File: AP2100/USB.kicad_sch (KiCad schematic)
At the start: 40 parts, among them IC9 MAX1564ETE+, J7 SS-52000-001, U10 LS1043ASE7KQB-Layerscape, U22 74LVC2G04

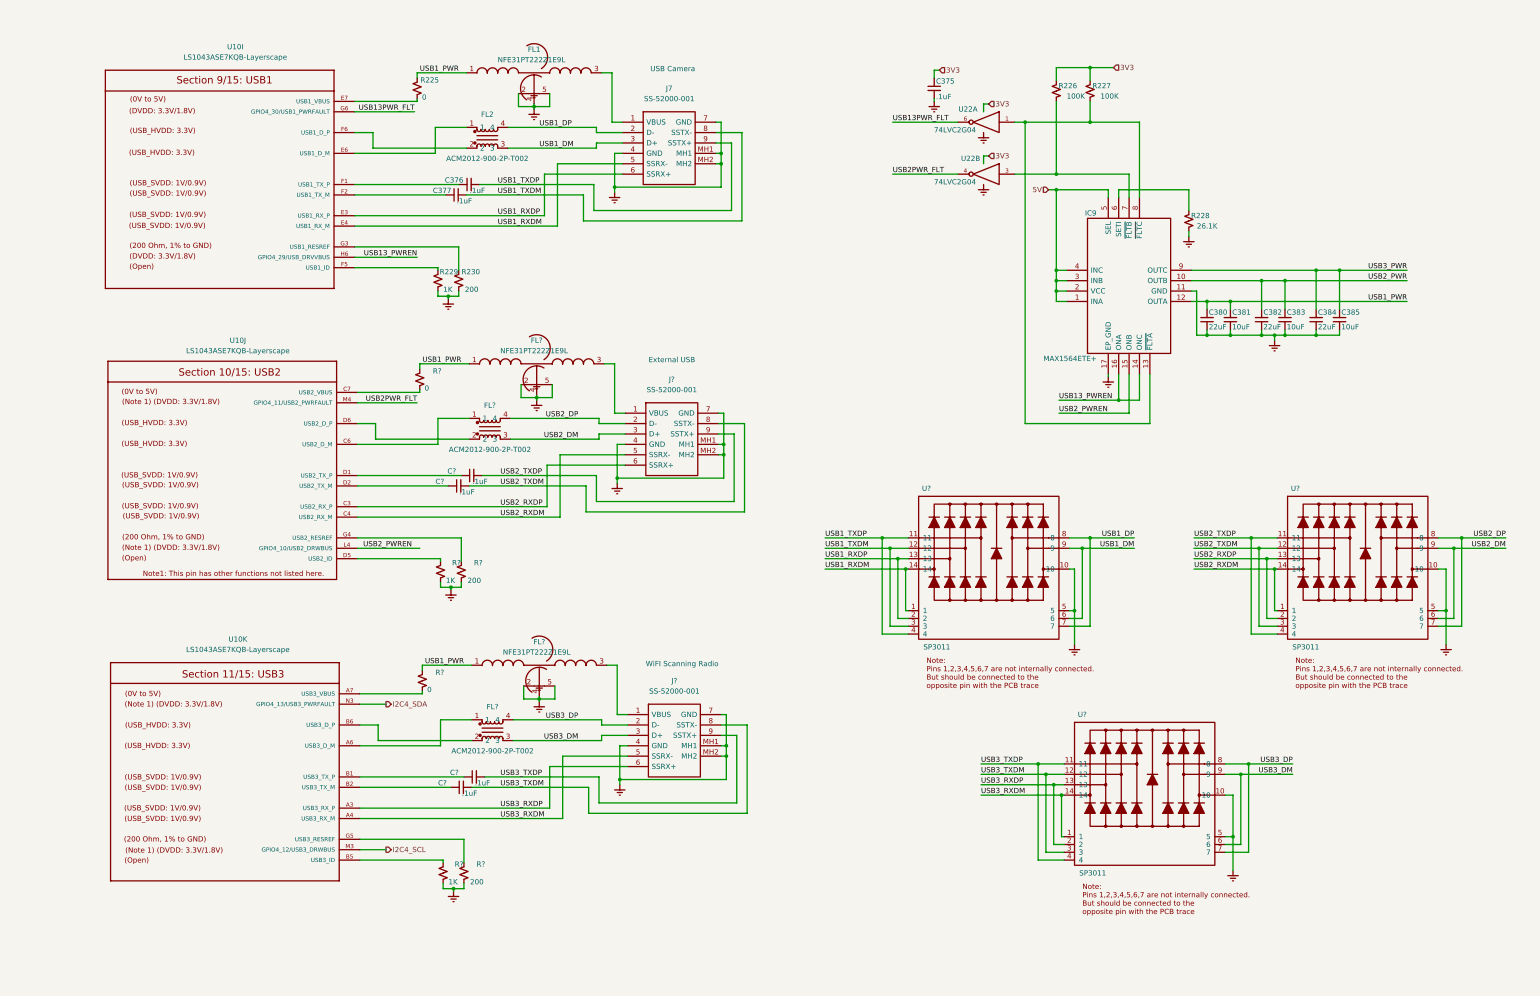
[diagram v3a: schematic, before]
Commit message: Review / cleanup footprints, etc
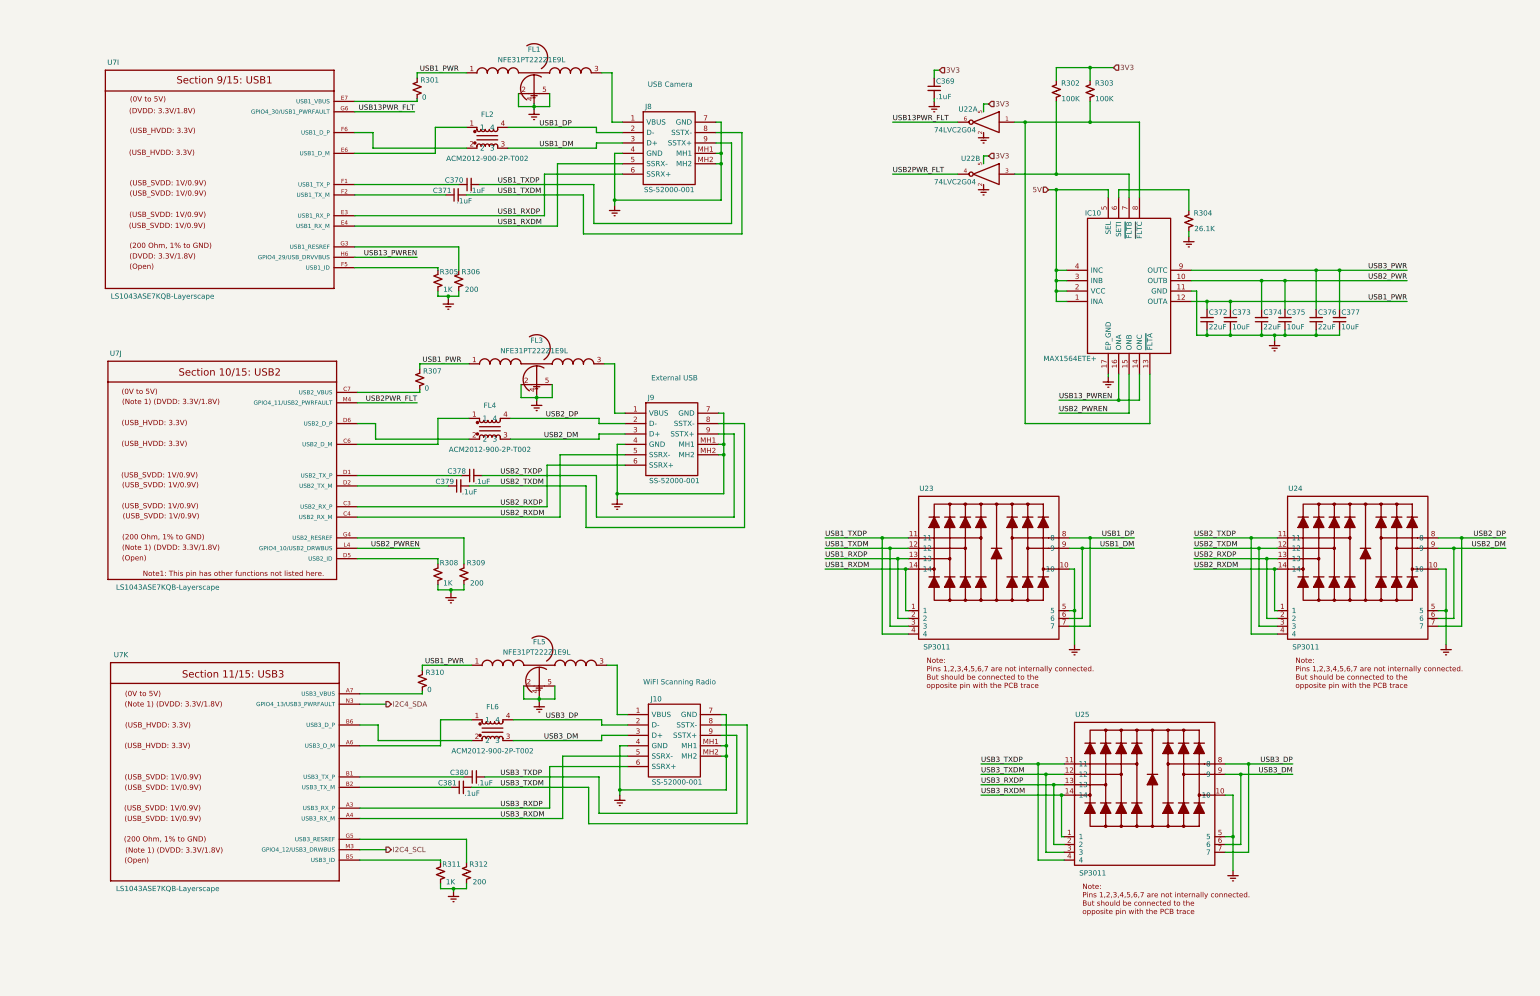
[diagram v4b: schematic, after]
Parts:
- U22: symbol 74xGxx:74LVC2G04 -> Scott:74LVC2G04
- gave numbers to parts that had none: 19
- renumbered C375 to C369, C376 to C370, C377 to C371, C380 to C372, C381 to C373, C382 to C374, C383 to C375, C384 to C376, C385 to C377, IC9 to IC10, J7 to J8, R225 to R301, R226 to R302, R227 to R303, R228 to R304, R229 to R305, R230 to R306, U10 to U7
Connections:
- net VCC renamed 3V3
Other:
- moved on the sheet: R308, R309, R311, R312

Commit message: Added antenna mounting holes
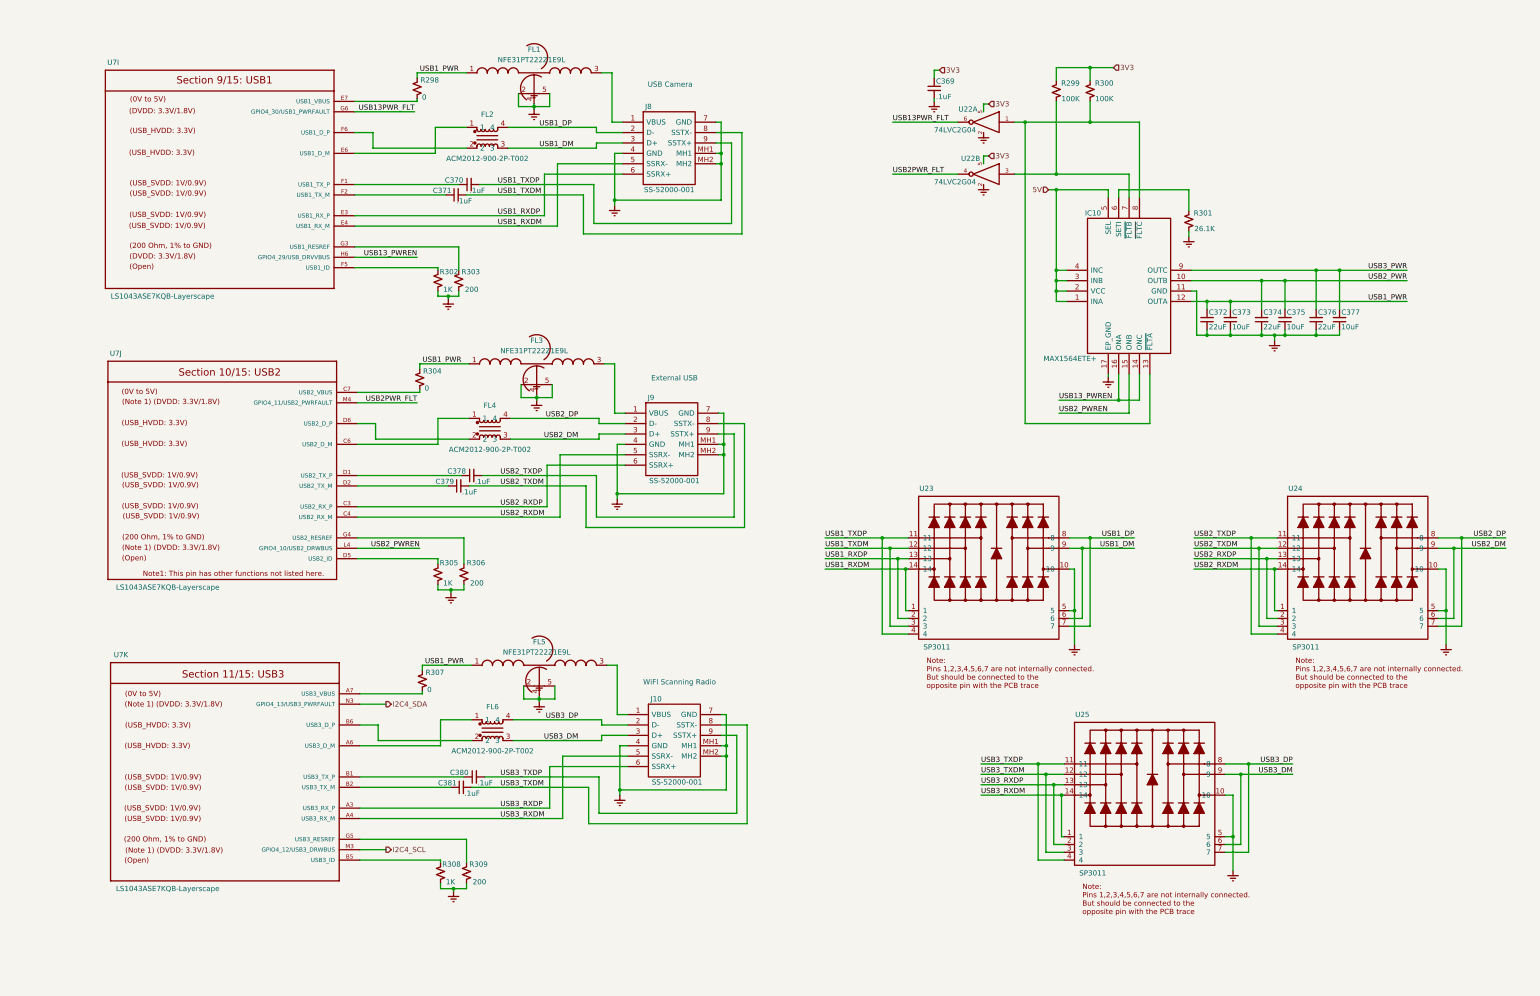
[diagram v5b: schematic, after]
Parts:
- renumbered R301 to R298, R302 to R299, R303 to R300, R304 to R301, R305 to R302, R306 to R303, R307 to R304, R308 to R305, R309 to R306, R310 to R307, R311 to R308, R312 to R309
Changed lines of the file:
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@@
   (symbol (lib_id "Device:R_Small_US") (at 131.445 41.91 0) (mirror y) (unit 1)
     (in_bom yes) (on_board yes)
-    (property "Reference" "R301" (id 0) (at 136.779 39.878 0)
+    (property "Reference" "R298" (id 0) (at 136.779 39.878 0)
       (effects (font (size 1.27 1.27)) (justify left))
     )
@@
   (symbol (lib_id "Device:R_Small_US") (at 132.08 113.03 0) (mirror y) (unit 1)
     (in_bom yes) (on_board yes)
-    (property "Reference" "R307" (id 0) (at 137.414 110.998 0)
+    (property "Reference" "R304" (id 0) (at 137.414 110.998 0)
       (effects (font (size 1.27 1.27)) (justify left))
     )
@@
   (symbol (lib_id "Device:R_Small_US") (at 132.715 186.69 0) (mirror y) (unit 1)
     (in_bom yes) (on_board yes)
-    (property "Reference" "R310" (id 0) (at 138.049 184.658 0)
+    (property "Reference" "R307" (id 0) (at 138.049 184.658 0)
       (effects (font (size 1.27 1.27)) (justify left))
     )
@@
   (symbol (lib_id "Device:R_Small_US") (at 136.525 88.9 0) (mirror y) (unit 1)
     (in_bom yes) (on_board yes)
-    (property "Reference" "R305" (id 0) (at 141.478 86.741 0)
+    (property "Reference" "R302" (id 0) (at 141.478 86.741 0)
       (effects (font (size 1.27 1.27)) (justify left))
     )
@@
   (symbol (lib_id "Device:R_Small_US") (at 136.525 160.655 0) (mirror y) (unit 1)
     (in_bom yes) (on_board yes)
-    (property "Reference" "R308" (id 0) (at 141.478 157.861 0)
+    (property "Reference" "R305" (id 0) (at 141.478 157.861 0)
       (effects (font (size 1.27 1.27)) (justify left))
     )
@@
   (symbol (lib_id "Device:R_Small_US") (at 137.16 233.68 0) (mirror y) (unit 1)
     (in_bom yes) (on_board yes)
-    (property "Reference" "R311" (id 0) (at 142.113 231.521 0)
+    (property "Reference" "R308" (id 0) (at 142.113 231.521 0)
       (effects (font (size 1.27 1.27)) (justify left))
     )
@@
   (symbol (lib_id "Device:R_Small_US") (at 141.605 88.9 0) (mirror y) (unit 1)
     (in_bom yes) (on_board yes)
-    (property "Reference" "R306" (id 0) (at 146.812 86.741 0)
+    (property "Reference" "R303" (id 0) (at 146.812 86.741 0)
       (effects (font (size 1.27 1.27)) (justify left))
     )
@@
   (symbol (lib_id "Device:R_Small_US") (at 142.875 160.655 0) (mirror y) (unit 1)
     (in_bom yes) (on_board yes)
-    (property "Reference" "R309" (id 0) (at 148.082 157.861 0)
+    (property "Reference" "R306" (id 0) (at 148.082 157.861 0)
       (effects (font (size 1.27 1.27)) (justify left))
     )
@@
   (symbol (lib_id "Device:R_Small_US") (at 143.51 233.68 0) (mirror y) (unit 1)
     (in_bom yes) (on_board yes)
-    (property "Reference" "R312" (id 0) (at 148.717 231.521 0)
+    (property "Reference" "R309" (id 0) (at 148.717 231.521 0)
       (effects (font (size 1.27 1.27)) (justify left))
     )
@@
   (symbol (lib_id "Device:R_Small_US") (at 287.655 42.545 0) (mirror y) (unit 1)
     (in_bom yes) (on_board yes)
-    (property "Reference" "R302" (id 0) (at 293.37 40.64 0)
+    (property "Reference" "R299" (id 0) (at 293.37 40.64 0)
       (effects (font (size 1.27 1.27)) (justify left))
     )
@@
   (symbol (lib_id "Device:R_Small_US") (at 295.91 42.545 0) (mirror y) (unit 1)
     (in_bom yes) (on_board yes)
-    (property "Reference" "R303" (id 0) (at 301.625 40.64 0)
+    (property "Reference" "R300" (id 0) (at 301.625 40.64 0)
       (effects (font (size 1.27 1.27)) (justify left))
     )
@@
   (symbol (lib_id "Device:R_Small_US") (at 320.04 74.295 0) (mirror y) (unit 1)
     (in_bom yes) (on_board yes)
-    (property "Reference" "R304" (id 0) (at 325.755 72.39 0)
-      (effects (font (size 1.27 1.27)) (justify left))
-    )
+    (property "Reference" "R301" (id 0) (at 325.755 72.39 0)
+      (effects (font (size 1.27 1.27)) (justify left))
+    )

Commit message: More cleanups
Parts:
- added R311, R312: 1K, Resistor_SMD:R_0402_1005Metric, symbol Device:R_Small_US
- renumbered C369 to C387, C370 to C388, C371 to C389, C372 to C390, C373 to C391, C374 to C392, C375 to C393, C376 to C394, C377 to C395, C378 to C396, C379 to C397, C380 to C398, C381 to C399, R298 to R299, R299 to R300, R300 to R301, R301 to R302, R302 to R303, R303 to R304, R304 to R305, R305 to R306, R306 to R307, R307 to R308, R308 to R309, R309 to R310
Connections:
- net 3V3: now also R311.2, R312.2
- net I2C4_SCL: now also R311.1
- net I2C4_SDA: now also R312.1

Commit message: Not sure
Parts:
- FL1, FL3, FL5: PartsBoxID (none) -> NFE31PT222Z1E9L
- FL2, FL4, FL6: PartsBoxID (none) -> ACM2012-900-2P-T002
- IC10: PartsBoxID (none) -> MAX1564ETE+
- J10, J8, J9: PartsBoxID (none) -> SS-52000-001
- U23, U24, U25: PartsBoxID (none) -> SP3011
- U7: value LS1043ASE7KQB-Layerscape -> LS1043ASE7xxx; PartsBoxID (none) -> LS1043ASE7
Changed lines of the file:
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@@
       (effects (font (size 1.27 1.27)) (justify left) hide)
+    )
+    (property "PartsBoxID" "ACM2012-900-2P-T002" (id 4) (at 148.59 53.975 0)
+      (effects (font (size 1.27 1.27)) hide)
     )
   )
@@
       (effects (font (size 1.27 1.27)) (justify left) hide)
     )
+    (property "PartsBoxID" "ACM2012-900-2P-T002" (id 4) (at 149.225 125.095 0)
+      (effects (font (size 1.27 1.27)) hide)
+    )
   )
   (symbol (lib_id "ACM2012-900-2P-T002:ACM2012-900-2P-T002") (at 149.86 198.755 0) (unit 1)
@@
       (effects (font (size 1.27 1.27)) (justify left) hide)
     )
+    (property "PartsBoxID" "ACM2012-900-2P-T002" (id 4) (at 149.86 198.755 0)
+      (effects (font (size 1.27 1.27)) hide)
+    )
   )
   (symbol (lib_name "Scott:74LVC2G04_1") (lib_id "Scott:74LVC2G04") (at 269.875 50.165 0) (mirror y) (unit 1)
@@
       (effects (font (size 1.27 1.27)) (justify left) hide)
     )
+    (property "PartsBoxID" "SS-52000-001" (id 4) (at 181.61 50.165 0)
+      (effects (font (size 1.27 1.27)) hide)
+    )
   )
   (symbol (lib_name "SS-52000-001:SS-52000-001_3") (lib_id "SS-52000-001:SS-52000-001") (at 182.245 121.285 0) (unit 1)
@@
       (effects (font (size 1.27 1.27)) (justify left) hide)
     )
+    (property "PartsBoxID" "SS-52000-001" (id 4) (at 182.245 121.285 0)
+      (effects (font (size 1.27 1.27)) hide)
+    )
   )
   (symbol (lib_id "SS-52000-001:SS-52000-001") (at 182.88 194.945 0) (unit 1)
@@
       (effects (font (size 1.27 1.27)) (justify left) hide)
     )
+    (property "PartsBoxID" "SS-52000-001" (id 4) (at 182.88 194.945 0)
+      (effects (font (size 1.27 1.27)) hide)
+    )
   )
   (symbol (lib_id "NFE31PT222Z1E9L:NFE31PT222Z1E9L") (at 143.51 38.1 0) (unit 1)
@@
       (effects (font (size 1.27 1.27)) (justify left) hide)
     )
+    (property "PartsBoxID" "NFE31PT222Z1E9L" (id 4) (at 143.51 38.1 0)
+      (effects (font (size 1.27 1.27)) hide)
+    )
   )
   (symbol (lib_id "NFE31PT222Z1E9L:NFE31PT222Z1E9L") (at 144.145 109.22 0) (unit 1)
@@
       (effects (font (size 1.27 1.27)) (justify left) hide)
     )
+    (property "PartsBoxID" "NFE31PT222Z1E9L" (id 4) (at 144.145 109.22 0)
+      (effects (font (size 1.27 1.27)) hide)
+    )
   )
   (symbol (lib_id "NFE31PT222Z1E9L:NFE31PT222Z1E9L") (at 144.78 182.88 0) (unit 1)
@@
       (effects (font (size 1.27 1.27)) (justify left) hide)
     )
+    (property "PartsBoxID" "NFE31PT222Z1E9L" (id 4) (at 144.78 182.88 0)
+      (effects (font (size 1.27 1.27)) hide)
+    )
   )
   (symbol (lib_id "MAX1564ETE+:MAX1564ETE+") (at 290.195 93.98 0) (mirror x) (unit 1)
@@
     (property "Mouser Price/Stock" "https://www.mouser.com/Search/Refine.aspx?Keyword=700-MAX1564ETE" (id 11) (at 316.865 83.82 0)
       (effects (font (size 1.27 1.27)) (justify left) hide)
+    )
+    (property "PartsBoxID" "MAX1564ETE+" (id 4) (at 290.195 93.98 0)
+      (effects (font (size 1.27 1.27)) hide)
     )
   )
@@
       (effects (font (size 1.27 1.27)) hide)
     )
+    (property "PartsBoxID" "SP3011" (id 4) (at 271.145 155.575 0)
+      (effects (font (size 1.27 1.27)) hide)
+    )
   )
   (symbol (lib_id "Scott:SP3011") (at 309.245 210.82 0) (unit 1)
@@
       (effects (font (size 1.27 1.27)) hide)
     )
+    (property "PartsBoxID" "SP3011" (id 4) (at 309.245 210.82 0)
+      (effects (font (size 1.27 1.27)) hide)
+    )
   )
   (symbol (lib_name "Scott:SP3011_2") (lib_id "Scott:SP3011") (at 361.315 155.575 0) (unit 1)
@@
       (effects (font (size 1.27 1.27)) hide)
     )
+    (property "PartsBoxID" "SP3011" (id 4) (at 361.315 155.575 0)
+      (effects (font (size 1.27 1.27)) hide)
+    )
   )
   (symbol (lib_id "AP2100-rescue:LS1043ASE7KQB-Layerscape") (at 83.185 208.915 0) (unit 11)
     (in_bom yes) (on_board yes)
     (property "Reference" "U7" (id 0) (at 59.055 180.34 0))
-    (property "Value" "LS1043ASE7KQB-Layerscape" (id 1) (at 70.485 237.49 0))
+    (property "Value" "LS1043ASE7xxx" (id 1) (at 70.485 237.49 0))
     (property "Footprint" "PLS1043ASE7QQA:BGA621C80P25X25_2100X2100X192N" (id 2) (at 83.185 208.915 0)
       (effects (font (size 1.27 1.27)) hide)
@@
       (effects (font (size 1.27 1.27)) hide)
     )
+    (property "PartsBoxID" "LS1043ASE7" (id 4) (at 83.185 208.915 0)
+      (effects (font (size 1.27 1.27)) hide)
+    )
   )
   (symbol (lib_id "AP2100-rescue:LS1043ASE7KQB-Layerscape") (at 85.09 133.985 0) (unit 10)
     (in_bom yes) (on_board yes)
     (property "Reference" "U7" (id 0) (at 57.785 106.68 0))
-    (property "Value" "LS1043ASE7KQB-Layerscape" (id 1) (at 70.485 163.83 0))
+    (property "Value" "LS1043ASE7xxx" (id 1) (at 70.485 163.83 0))
     (property "Footprint" "PLS1043ASE7QQA:BGA621C80P25X25_2100X2100X192N" (id 2) (at 85.09 133.985 0)
       (effects (font (size 1.27 1.27)) hide)
@@
       (effects (font (size 1.27 1.27)) hide)
     )
+    (property "PartsBoxID" "LS1043ASE7" (id 4) (at 85.09 133.985 0)
+      (effects (font (size 1.27 1.27)) hide)
+    )
   )
   (symbol (lib_id "AP2100-rescue:LS1043ASE7KQB-Layerscape") (at 85.725 62.865 0) (unit 9)
     (in_bom yes) (on_board yes)
     (property "Reference" "U7" (id 0) (at 57.15 35.56 0))
-    (property "Value" "LS1043ASE7KQB-Layerscape" (id 1) (at 69.215 92.71 0))
+    (property "Value" "LS1043ASE7xxx" (id 1) (at 69.215 92.71 0))
     (property "Footprint" "PLS1043ASE7QQA:BGA621C80P25X25_2100X2100X192N" (id 2) (at 85.725 62.865 0)
       (effects (font (size 1.27 1.27)) hide)
@@
       (effects (font (size 1.27 1.27)) hide)
     )
+    (property "PartsBoxID" "LS1043ASE7" (id 4) (at 85.725 62.865 0)
+      (effects (font (size 1.27 1.27)) hide)
+    )
